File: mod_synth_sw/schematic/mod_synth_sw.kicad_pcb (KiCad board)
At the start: 2 copper layers, 43 parts, among them J1 Conn_02x08_Odd_Even, J2 CLK, J3 RST, J4 I/O, J5 I/O 1, J6 I/O 2, J7 I/O 3, J8 I/O 4, Q1 2N3904, Q2 2N3904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

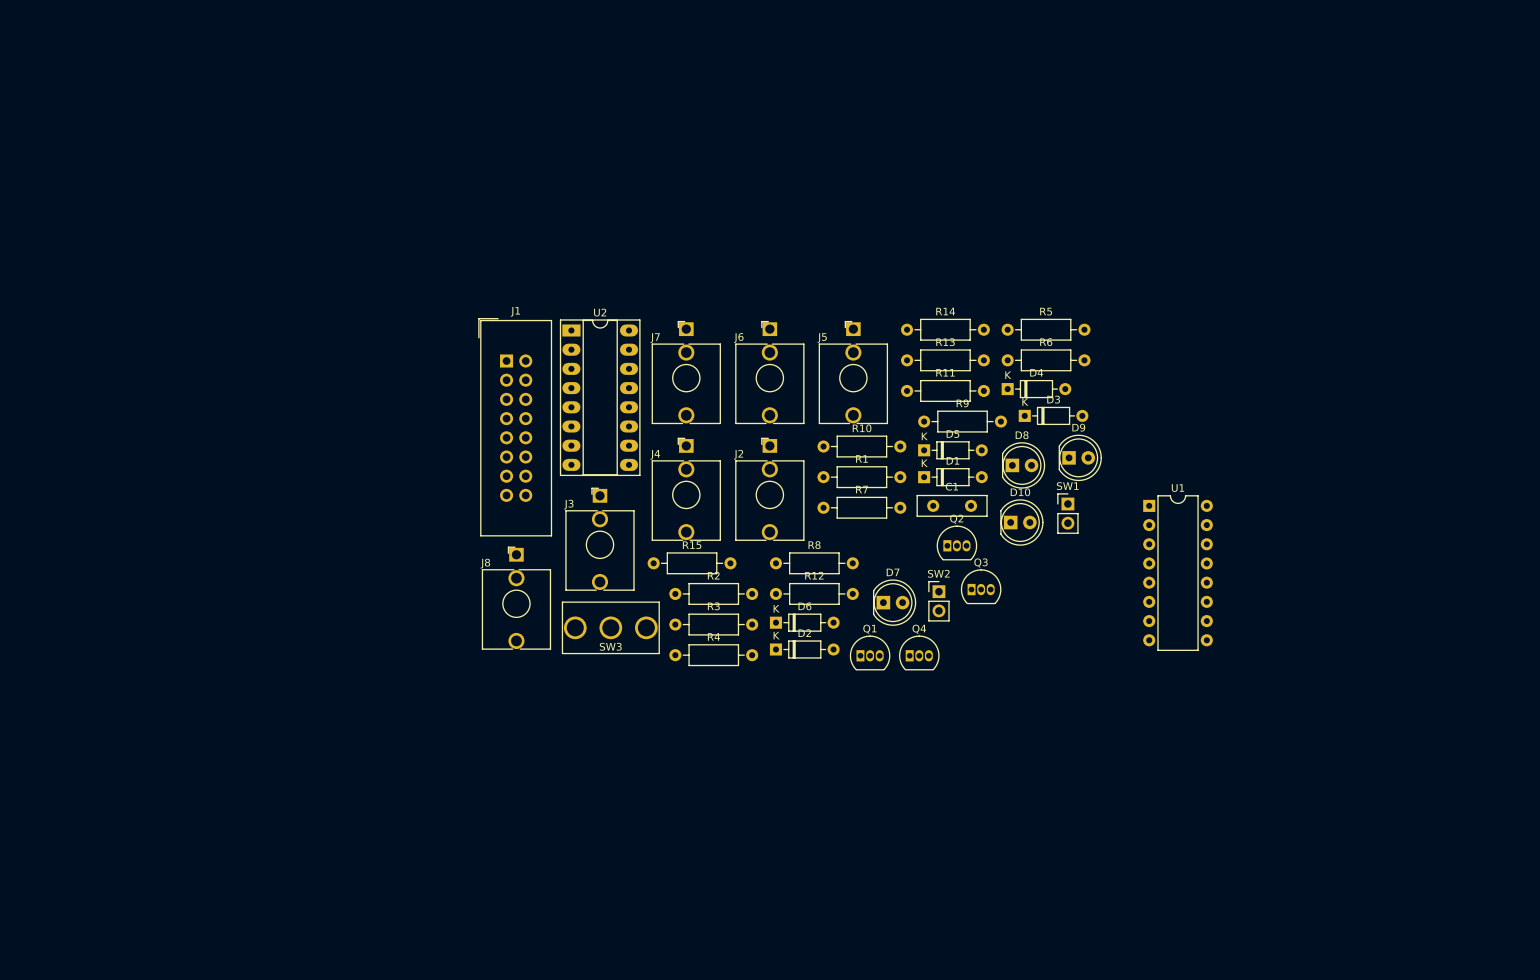
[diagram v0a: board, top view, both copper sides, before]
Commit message: Group some components in PCB
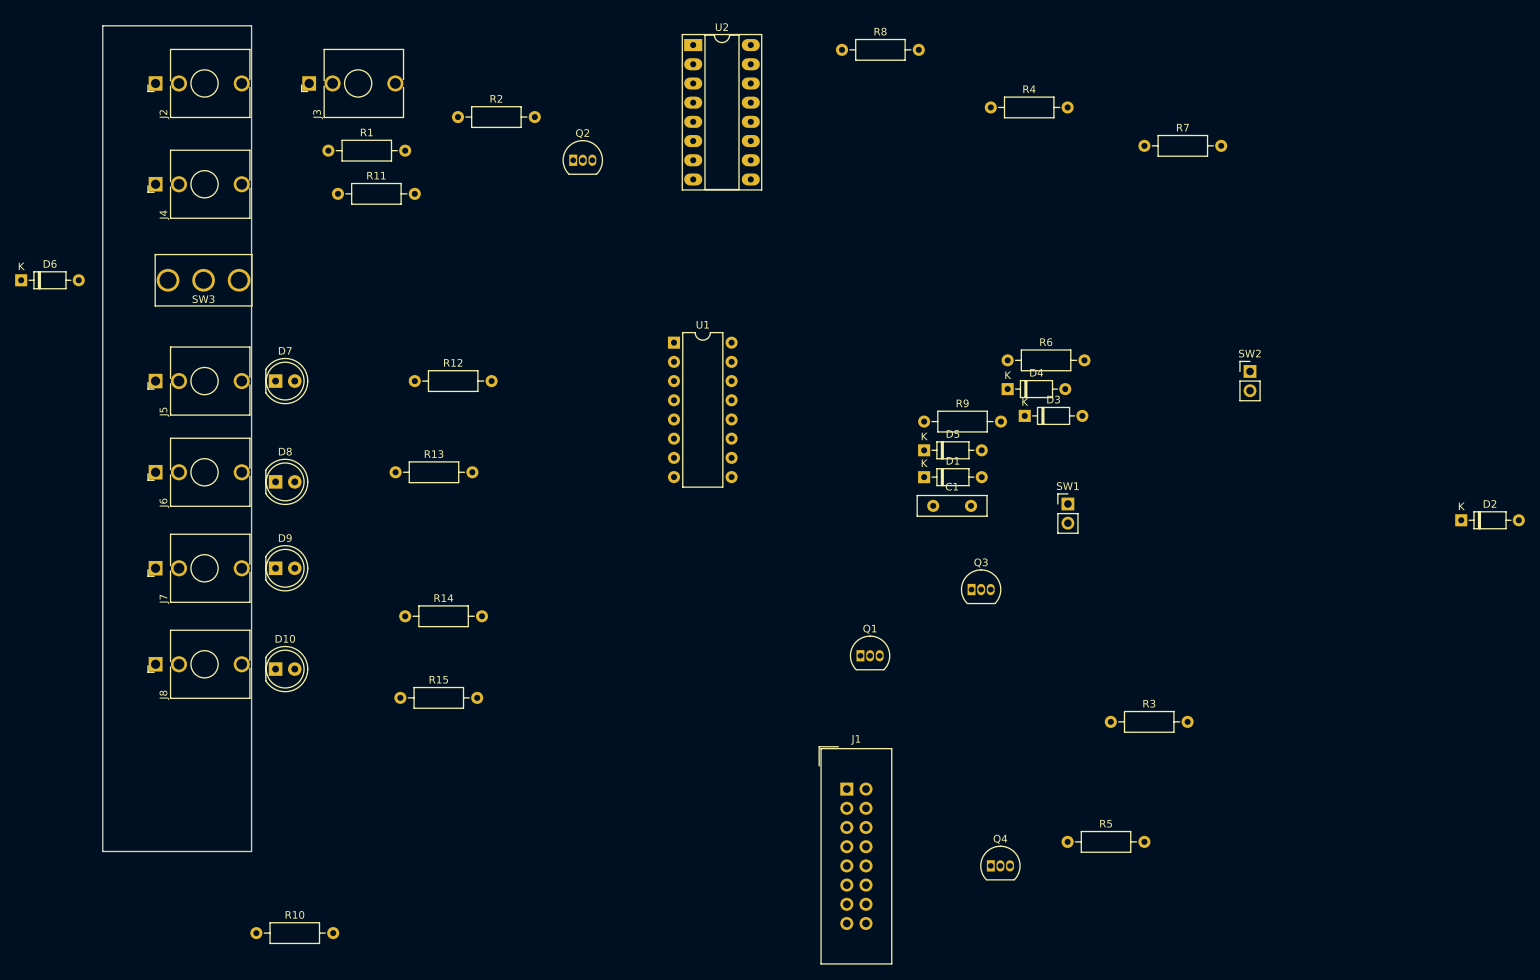
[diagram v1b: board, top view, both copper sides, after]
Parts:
- moved D6 109.6 mm to (13.3, 75.6)
- moved D9 106.0 mm to (47.0, 113.7)
- moved D10 99.2 mm to (47.0, 127.0)
- moved R10 98.9 mm to (44.5, 161.9)
- moved D8 97.5 mm to (47.0, 102.2)
- moved J2 94.4 mm to (31.1, 49.5), turned to 90 degrees
- moved J5 92.6 mm to (31.1, 88.9), turned to 90 degrees
- moved D2 92.2 mm to (203.8, 107.3)
- moved D7 85.6 mm to (47.0, 88.9)
- moved R4 83.6 mm to (141.6, 52.7)
- moved J6 83.4 mm to (31.1, 101.0), turned to 90 degrees
- moved R11 79.7 mm to (55.2, 64.1)
- moved R1 78.5 mm to (54.0, 58.4)
- moved J4 78.3 mm to (31.1, 62.9), turned to 90 degrees
- moved J7 77.0 mm to (31.1, 113.7), turned to 90 degrees
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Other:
- board outline added: 19.7 x 109.2 mm

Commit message: Layout some tracks
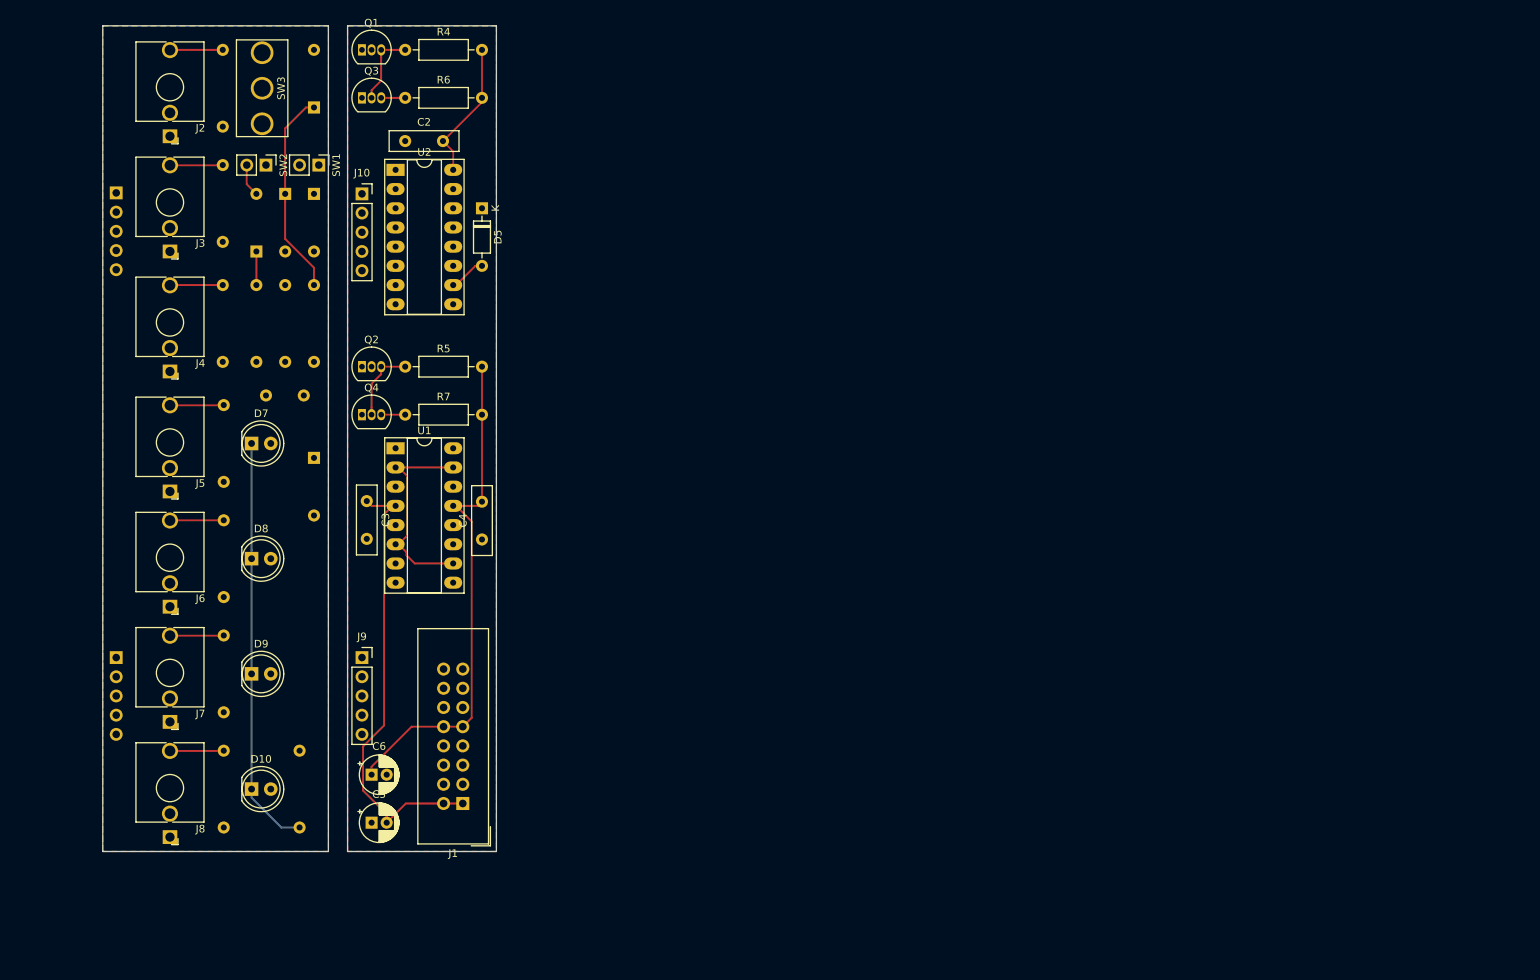
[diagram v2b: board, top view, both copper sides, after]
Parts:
- added C2: 100nf, Capacitor_THT:C_Disc_D9.0mm_W2.5mm_P5.00mm, F.Cu at (64.1, 57.1)
- added C3: 100nf, Capacitor_THT:C_Disc_D9.0mm_W2.5mm_P5.00mm, F.Cu at (59.1, 104.8)
- added C4: 100nf, Capacitor_THT:C_Disc_D9.0mm_W2.5mm_P5.00mm, F.Cu at (74.3, 109.9)
- added C5: 10uf, Capacitor_THT:CP_Radial_D5.0mm_P2.00mm, F.Cu at (59.7, 147.3)
- added C6: 10uf, Capacitor_THT:CP_Radial_D5.0mm_P2.00mm, F.Cu at (59.7, 141.0)
- added J10: Conn_01x05_Female, Connector_PinSocket_2.54mm:PinSocket_1x05_P2.54mm_Vertical, F.Cu at (58.4, 64.1)
- added J11: Conn_01x05_Male, Connector_PinHeader_2.54mm:PinHeader_1x05_P2.54mm_Vertical, B.Cu at (25.9, 64.0)
- added J12: Conn_01x05_Male, Connector_PinHeader_2.54mm:PinHeader_1x05_P2.54mm_Vertical, B.Cu at (25.9, 125.5)
- added J9: Conn_01x05_Female, Connector_PinSocket_2.54mm:PinSocket_1x05_P2.54mm_Vertical, F.Cu at (58.4, 125.5)
- C1, D1, D2, D3, D4, D6, R1, R10, R11, R12, R13, R14, R15, R2, R3, R8, R9: moved to B.Cu
- U1: footprint Package_DIP:DIP-16_W7.62mm -> Package_DIP:DIP-16_W7.62mm_Socket_LongPads
- moved D2 161.5 mm to (48.3, 64.1), turned to 270 degrees
- moved SW2 133.0 mm to (45.7, 60.3), turned to 270 degrees
- moved R3 123.6 mm to (48.3, 76.2), turned to 270 degrees
- moved SW1 108.8 mm to (52.7, 60.3), turned to 270 degrees
- moved R5 107.8 mm to (64.1, 87.0)
- moved R7 104.1 mm to (64.1, 93.3)
- moved D3 103.9 mm to (44.5, 71.8), turned to 90 degrees
- moved Q1 103.8 mm to (58.4, 45.1)
- moved Q3 103.6 mm to (58.4, 51.4)
- moved Q4 102.4 mm to (58.4, 93.3)
- moved D4 95.3 mm to (52.1, 64.1), turned to 270 degrees
- moved D1 94.4 mm to (52.1, 52.7), turned to 90 degrees
- moved C1 89.5 mm to (45.7, 90.8)
- moved R6 86.9 mm to (64.1, 51.4)
- moved R8 83.5 mm to (44.5, 76.2), turned to 270 degrees
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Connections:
- J1 pad 1: Net-(J1-Pad1) -> -12V
- J1 pad 10: Net-(J1-Pad10) -> +12V
- J1 pad 2: Net-(J1-Pad2) -> -12V
- J1 pad 3: Net-(J1-Pad3) -> GND
- J1 pad 5: Net-(J1-Pad5) -> GND
- J1 pad 6: Net-(J1-Pad6) -> Net-(J1-Pad4)
- J1 pad 7: Net-(J1-Pad7) -> GND
- J1 pad 8: Net-(J1-Pad8) -> Net-(J1-Pad4)
- J1 pad 9: Net-(J1-Pad9) -> +12V
- J2 pad S: GND -> /GND_PCB_B
- J3 pad S: GND -> /GND_PCB_B
- J4 pad S: GND -> /GND_PCB_B
- J5 pad S: GND -> /GND_PCB_B
- J6 pad S: GND -> /GND_PCB_B
- J7 pad S: GND -> /GND_PCB_B
- J8 pad S: GND -> /GND_PCB_B
- R10 pad 1: GND -> /GND_PCB_B
- U1 pad 13: Net-(U1-Pad13) -> +12V
- U1 pad 4: Net-(U1-Pad4) -> -12V
- U1 pad 5: Net-(U1-Pad5) -> GND
- U2 pad 16: Net-(U2-Pad16) -> +12V
- U2 pad 8: Net-(U2-Pad8) -> GND
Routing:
- net +12V: track 0.00 -> 86.7 mm
- net -12V: track 0.00 -> 60.4 mm
- net Net-(D10-Pad1): track 0.00 -> 54.8 mm
- net Net-(R11-Pad2): track 0.00 -> 28.0 mm
- net Net-(D1-Pad1): track 0.00 -> 27.3 mm
- net Net-(Q1-Pad3): track 0.00 -> 10.1 mm
- net Net-(Q2-Pad3): track 0.00 -> 10.1 mm
- net Net-(J6-PadT): track 0.00 -> 7.12 mm
- net Net-(J8-PadT): track 0.00 -> 7.12 mm
- net Net-(J5-PadT): track 0.00 -> 7.12 mm
- net Net-(J7-PadT): track 0.00 -> 7.12 mm
- net Net-(J4-PadT): track 0.00 -> 7.00 mm
- net Net-(J2-PadT): track 0.00 -> 7.00 mm
- net Net-(J3-PadT): track 0.00 -> 7.00 mm
- net Net-(D5-Pad2): track 0.00 -> 4.86 mm
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- added copper zone on F.Cu, net /GND_PCB_B
- added copper zone on F.Cu, net GND
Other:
- board size 19.7 x 109.2 mm -> 52.1 x 109.2 mm

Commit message: Enlarge second PCB
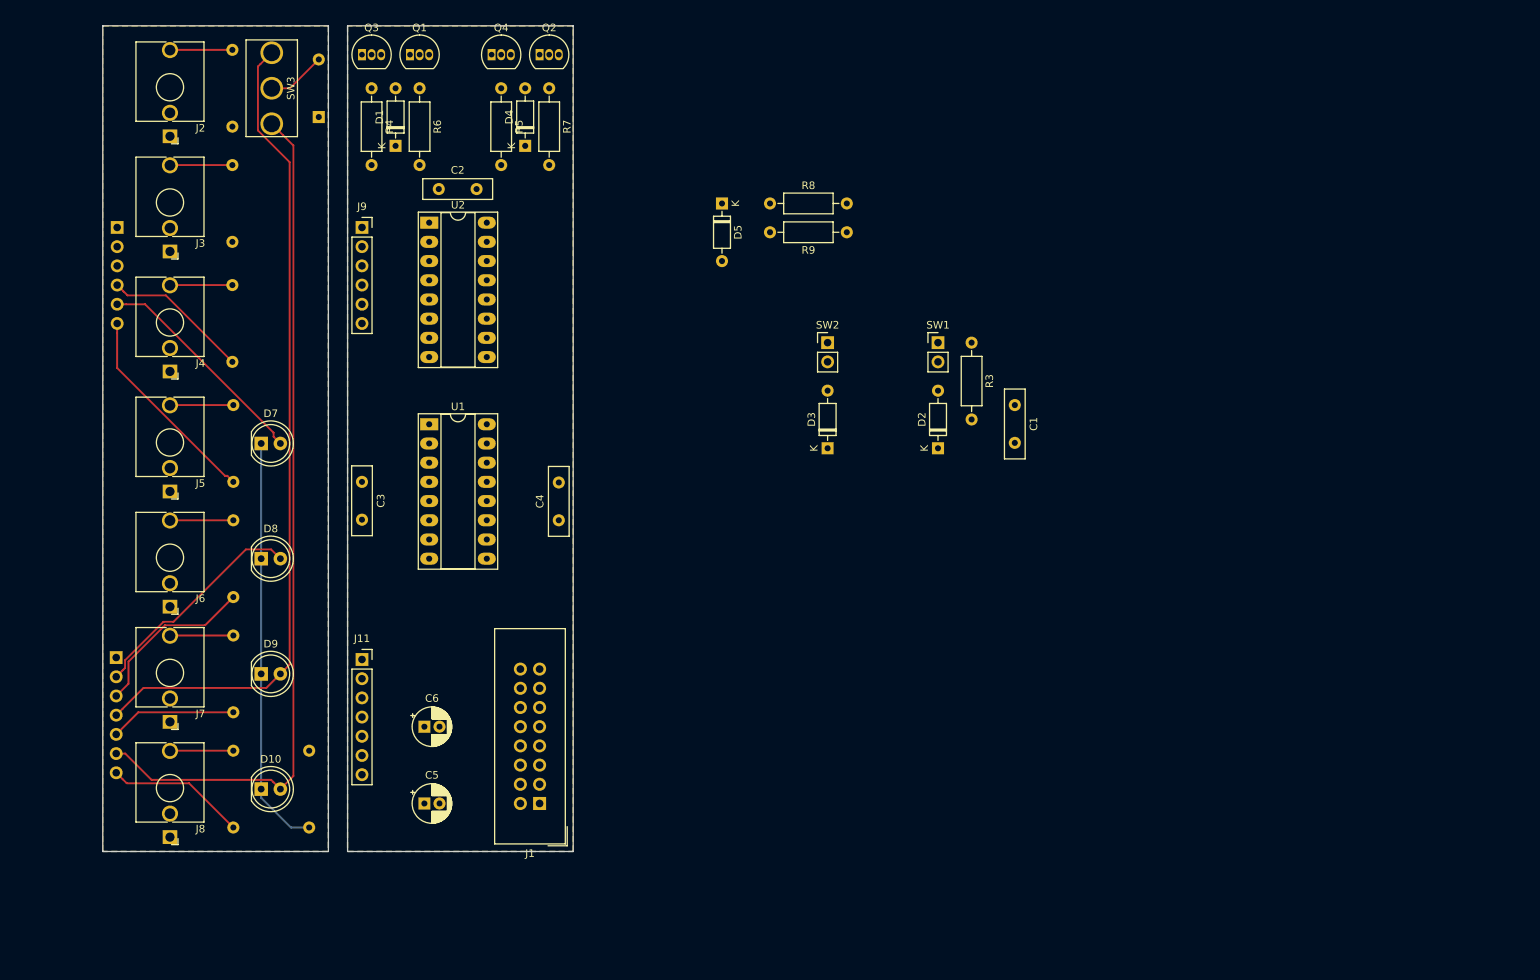
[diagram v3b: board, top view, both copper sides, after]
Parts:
- C1, D1, D2, D3, D4, R3, R8, R9: moved to F.Cu
- J10: renamed from J11; value Conn_01x05_Male -> Conn_01x06_Male; footprint Connector_PinHeader_2.54mm:PinHeader_1x05_P2.54mm_Vertical -> Connector_PinHeader_2.54mm:PinHeader_1x06_P2.54mm_Vertical
- J11: renamed from J10; value Conn_01x05_Female -> Conn_01x07_Female; footprint Connector_PinSocket_2.54mm:PinSocket_1x05_P2.54mm_Vertical -> Connector_PinSocket_2.54mm:PinSocket_1x07_P2.54mm_Vertical
- J12: value Conn_01x05_Male -> Conn_01x07_Male; footprint Connector_PinHeader_2.54mm:PinHeader_1x05_P2.54mm_Vertical -> Connector_PinHeader_2.54mm:PinHeader_1x07_P2.54mm_Vertical
- J9: value Conn_01x05_Female -> Conn_01x06_Female; footprint Connector_PinSocket_2.54mm:PinSocket_1x05_P2.54mm_Vertical -> Connector_PinSocket_2.54mm:PinSocket_1x06_P2.54mm_Vertical
- moved C1 99.1 mm to (144.8, 92.1), turned to 270 degrees
- moved D2 92.7 mm to (134.6, 97.8), turned to 90 degrees
- moved R3 91.1 mm to (139.1, 83.8)
- moved SW1 85.2 mm to (134.6, 83.8), turned to 0 degrees
- moved D3 79.9 mm to (120.0, 97.8)
- moved SW2 77.9 mm to (120.0, 83.8), turned to 0 degrees
- moved R9 72.5 mm to (122.6, 69.2), turned to 180 degrees
- moved R8 68.8 mm to (112.4, 65.4), turned to 0 degrees
- moved J11 61.6 mm to (58.4, 125.7)
- moved J9 56.9 mm to (58.4, 68.6)
- moved Q4 50.6 mm to (75.6, 45.7)
- moved Q2 47.5 mm to (81.9, 45.7)
- moved R7 47.2 mm to (83.2, 50.2), turned to 270 degrees
- moved D6 45.1 mm to (52.7, 54.0), turned to 90 degrees
- moved R5 39.0 mm to (76.8, 50.2), turned to 270 degrees
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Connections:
- D10 pad 2: Net-(D10-Pad2) -> /LED_4_PCB_B
- D3 pad 1: Net-(D3-Pad1) -> /SW_RST_PCB_A
- D4 pad 1: Net-(D3-Pad1) -> /SW_RST_PCB_A
- D5 pad 1: Net-(D3-Pad1) -> /SW_RST_PCB_A
- D6 pad 1: Net-(D3-Pad1) -> /SW_RST_PCB_B
- D7 pad 2: Net-(D7-Pad2) -> /LED_1_PCB_B
- D8 pad 2: Net-(D8-Pad2) -> /LED_2_PCB_B
- D9 pad 2: Net-(D9-Pad2) -> /LED_3_PCB_B
- J1 pad 4: Net-(J1-Pad4) -> GND
- J1 pad 6: Net-(J1-Pad4) -> GND
- J1 pad 8: Net-(J1-Pad4) -> GND
- J10 pad 4: Net-(J11-Pad4) -> /0_PCB_B
- J10 pad 5: Net-(J11-Pad5) -> /LED_1_PCB_B
- J11 pad 2: Net-(J10-Pad2) (its old number) -> /LED_2_PCB_A
- J11 pad 3: Net-(J10-Pad3) (its old number) -> /2_PCB_A
- J11 pad 4: Net-(J10-Pad4) -> /LED_3_PCB_A
- J11 pad 5: Net-(J10-Pad5) -> /3_PCB_A
- J12 pad 2: Net-(J12-Pad2) -> /LED_2_PCB_B
- J12 pad 3: Net-(J12-Pad3) -> /2_PCB_B
- J12 pad 4: Net-(J12-Pad4) -> /LED_3_PCB_B
- J12 pad 5: Net-(J12-Pad5) -> /3_PCB_B
- J9 pad 4: Net-(J9-Pad4) -> /0_PCB_A
- J9 pad 5: Net-(J9-Pad5) -> /LED_1_PCB_A
- Q1 pad 2: Net-(Q1-Pad2) -> /CLK_PCB_A
- Q2 pad 2: Net-(Q2-Pad2) -> /RST_PCB_A
- R1 pad 1: Net-(Q1-Pad2) -> /CLK_PCB_B
- R11 pad 2: Net-(R11-Pad2) -> /0_PCB_B
- R12 pad 2: Net-(R12-Pad2) -> /1_PCB_B
- R13 pad 2: Net-(R13-Pad2) -> /2_PCB_B
- R14 pad 2: Net-(R14-Pad2) -> /3_PCB_B
- R15 pad 2: Net-(R15-Pad2) -> /4_PCB_B
- R2 pad 1: Net-(Q2-Pad2) -> /RST_PCB_B
- R8 pad 1: Net-(D3-Pad1) -> /SW_RST_PCB_A
- SW3 pad 1: Net-(D10-Pad2) -> /LED_4_PCB_B
- SW3 pad 3: Net-(D9-Pad2) -> /LED_3_PCB_B
- U1 pad 1: Net-(D7-Pad2) -> /LED_1_PCB_A
- U1 pad 10: Net-(R11-Pad2) -> /0_PCB_A
- U1 pad 11: Net-(R14-Pad2) -> /3_PCB_A
- U1 pad 14: Net-(R15-Pad2) -> /4_PCB_A
- U1 pad 15: Net-(R11-Pad2) -> /0_PCB_A
- U1 pad 16: Net-(D10-Pad2) -> /LED_4_PCB_A
- U1 pad 2: Net-(R11-Pad2) -> /0_PCB_A
- U1 pad 3: Net-(R12-Pad2) -> /1_PCB_A
- U1 pad 6: Net-(R11-Pad2) -> /0_PCB_A
- U1 pad 7: Net-(R13-Pad2) -> /2_PCB_A
- U1 pad 8: Net-(D8-Pad2) -> /LED_2_PCB_A
- U1 pad 9: Net-(D9-Pad2) -> /LED_3_PCB_A
- U2 pad 15: Net-(D3-Pad1) -> /SW_RST_PCB_A
- U2 pad 2: Net-(D8-Pad2) -> /LED_2_PCB_A
- U2 pad 3: Net-(D7-Pad2) -> /LED_1_PCB_A
- U2 pad 4: Net-(D9-Pad2) -> /LED_3_PCB_A
- U2 pad 7: Net-(D10-Pad2) -> /LED_4_PCB_A
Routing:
- net /LED_4_PCB_B: track 0.00 -> 113.6 mm
- net /LED_3_PCB_B: track 0.00 -> 109.1 mm
- net +12V: track 86.7 -> 0.00 mm
- net -12V: track 60.4 -> 0.00 mm
- net /LED_2_PCB_B: track 0.00 -> 29.8 mm
- net /LED_1_PCB_B: track 0.00 -> 29.5 mm
- net Net-(R11-Pad2): track 28.0 -> 0.00 mm
- net /1_PCB_B: track 0.00 -> 27.5 mm
- net Net-(D1-Pad1): track 27.3 -> 0.00 mm
- net /2_PCB_B: track 0.00 -> 22.6 mm
- net /0_PCB_B: track 0.00 -> 19.4 mm
- net /4_PCB_B: track 0.00 -> 18.5 mm
- net /3_PCB_B: track 0.00 -> 16.7 mm
- net Net-(Q1-Pad3): track 10.1 -> 0.00 mm
- net Net-(Q2-Pad3): track 10.1 -> 0.00 mm
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- added copper zone on B.Cu, net /GND_PCB_B
- added copper zone on B.Cu, net GND
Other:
- board size 52.1 x 109.2 mm -> 62.2 x 109.2 mm

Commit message: Complete PCB layout
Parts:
- moved R3 78.9 mm to (62.9, 63.5)
- moved C1 76.2 mm to (68.6, 90.2), turned to 0 degrees
- moved D2 76.2 mm to (59.1, 88.3), turned to 270 degrees
- moved SW1 72.2 mm to (62.9, 91.4)
- moved R9 43.6 mm to (79.4, 63.5), turned to 270 degrees
- moved SW2 41.3 mm to (79.4, 91.4)
- moved D3 38.0 mm to (83.2, 88.3), turned to 270 degrees
- moved R8 30.4 mm to (83.2, 73.7), turned to 90 degrees
- moved D5 25.3 mm to (83.2, 76.2)
- moved C6 1.91 mm to (68.6, 134.6), turned to 180 degrees
- moved D6 0.63 mm to (52.1, 54.0)
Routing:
- net +12V: track 0.00 -> 144.1 mm
- net /LED_3_PCB_A: track 0.00 -> 72.5 mm, vias 0 -> 1
- net -12V: track 0.00 -> 70.1 mm, vias 0 -> 1
- net /LED_2_PCB_A: track 0.00 -> 67.1 mm
- net /LED_4_PCB_A: track 0.00 -> 67.0 mm, vias 0 -> 1
- net /4_PCB_A: track 0.00 -> 64.4 mm
- net Net-(D1-Pad1): track 0.00 -> 59.6 mm
- net /0_PCB_A: track 0.00 -> 54.2 mm
- net /SW_RST_PCB_A: track 0.00 -> 46.5 mm
- net /3_PCB_A: track 0.00 -> 36.9 mm
- net /LED_1_PCB_A: track 0.00 -> 34.3 mm
- net Net-(R3-Pad1): track 0.00 -> 28.9 mm
- net /2_PCB_A: track 0.00 -> 25.9 mm
- net /1_PCB_A: track 0.00 -> 23.7 mm
- net Net-(Q2-Pad3): track 0.00 -> 13.7 mm
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
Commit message: Add missing connections
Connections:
- J10 pad 1: Net-(J10-Pad1) -> /CLK_PCB_B
- J10 pad 2: Net-(J10-Pad2) -> /RST_PCB_B
- J10 pad 3: Net-(J10-Pad3) -> /SW_RST_PCB_B
- J9 pad 1: Net-(J9-Pad1) -> /CLK_PCB_A
- J9 pad 2: Net-(J9-Pad2) -> /RST_PCB_A
- J9 pad 3: Net-(J9-Pad3) -> /SW_RST_PCB_A
- U1 pad 12: Net-(U1-Pad12) -> +12V
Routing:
- net /RST_PCB_A: track 0.00 -> 37.0 mm
- net /SW_RST_PCB_B: track 0.00 -> 35.6 mm
- net /CLK_PCB_A: track 0.00 -> 26.0 mm
- net /SW_RST_PCB_A: track 46.5 -> 71.6 mm
- net /CLK_PCB_B: track 0.00 -> 22.7 mm
- net /RST_PCB_B: track 0.00 -> 15.5 mm
- net +12V: track 144.1 -> 147.4 mm
- net /GND_PCB_B: vias 0 -> 1
